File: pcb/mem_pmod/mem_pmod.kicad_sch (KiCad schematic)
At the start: 0 parts

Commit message: Start building schematic
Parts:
- added J1: Conn_01x04_Pin, symbol Connector:Conn_01x04_Pin
- added PMOD1: PMOD-Device-x2-Type-1A-GPIO, pmod-conn_6x2:pmod_pin_array_6x2, symbol pmod:PMOD-Device-x2-Type-1A-GPIO
- added U1: 74ACT139MTCX, TSSOP16_5X4P5_ONS, symbol demux:74ACT139MTCX
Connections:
- new net CS_A0: J1.2 (Pin_2), U1.2 (A0A)
- new net CS_A1: J1.3 (Pin_3), U1.3 (A1A)
- new net CS_V0: J1.4 (Pin_4), U1.14 (A0B)
- new net GND: PMOD1.11 (GND), PMOD1.5 (GND), U1.13 (A1B), U1.8 (GND)
- new net PMOD_A0: PMOD1.1 (IOA0)
- new net PMOD_A1: PMOD1.2 (IOA1)
- new net PMOD_A2: PMOD1.3 (IOA2)
- new net PMOD_A3: PMOD1.4 (IOA3)
- new net PMOD_B0: PMOD1.7 (IOB0)
- new net PMOD_B1: PMOD1.8 (IOB1)
- new net PMOD_B2: PMOD1.9 (IOB2)
- new net PMOD_B3: PMOD1.10 (IOB3)
- new net PRJ_Clock: J1.1 (Pin_1)
- new net RAM_CS0: U1.4 (*O0A)
- new net RAM_CS1: U1.5 (*O1A)
- new net RAM_CS2: U1.6 (*O2A)
- new net RAM_CS3: U1.7 (*O3A)
- new net VCC: PMOD1.12 (VCC), PMOD1.6 (VCC), U1.1 (*EA), U1.15 (*EB), U1.16 (VCC)
- new net VRAM_CS0: U1.12 (*O0B)
- new net VRAM_CS1: U1.11 (*O1B)
- no-connect marks 0 -> 2

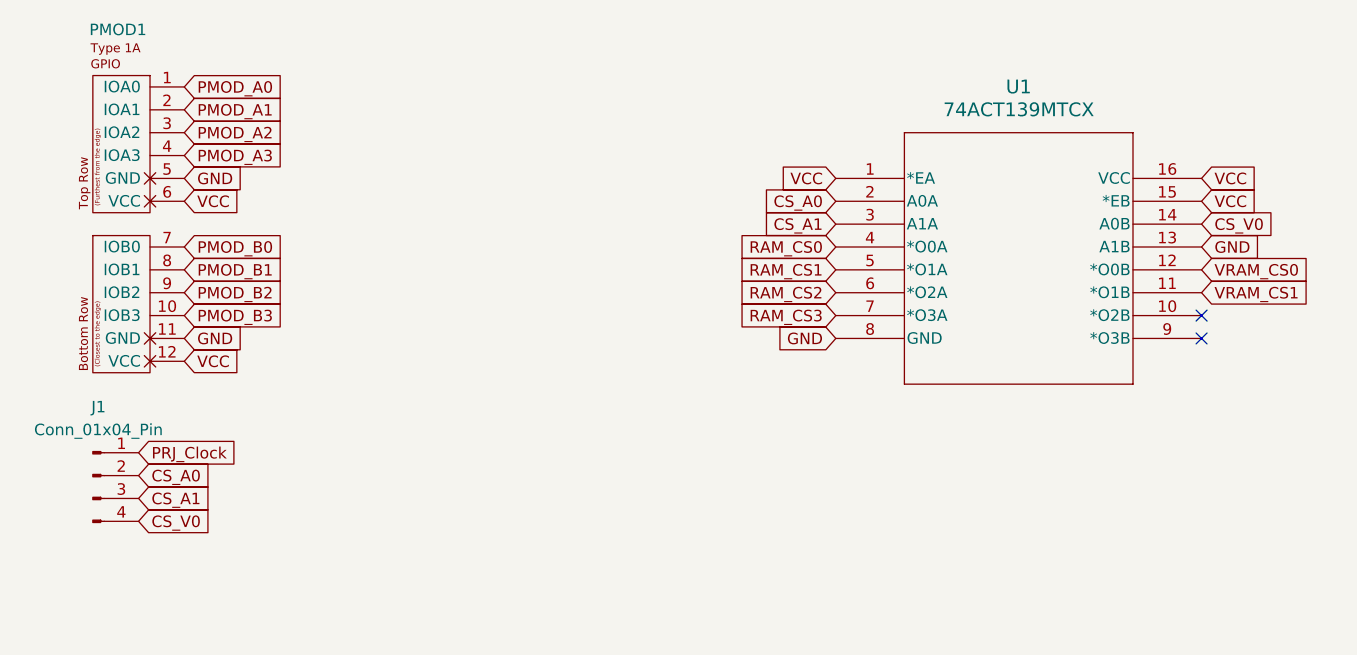
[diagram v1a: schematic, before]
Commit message: continue editing schematic
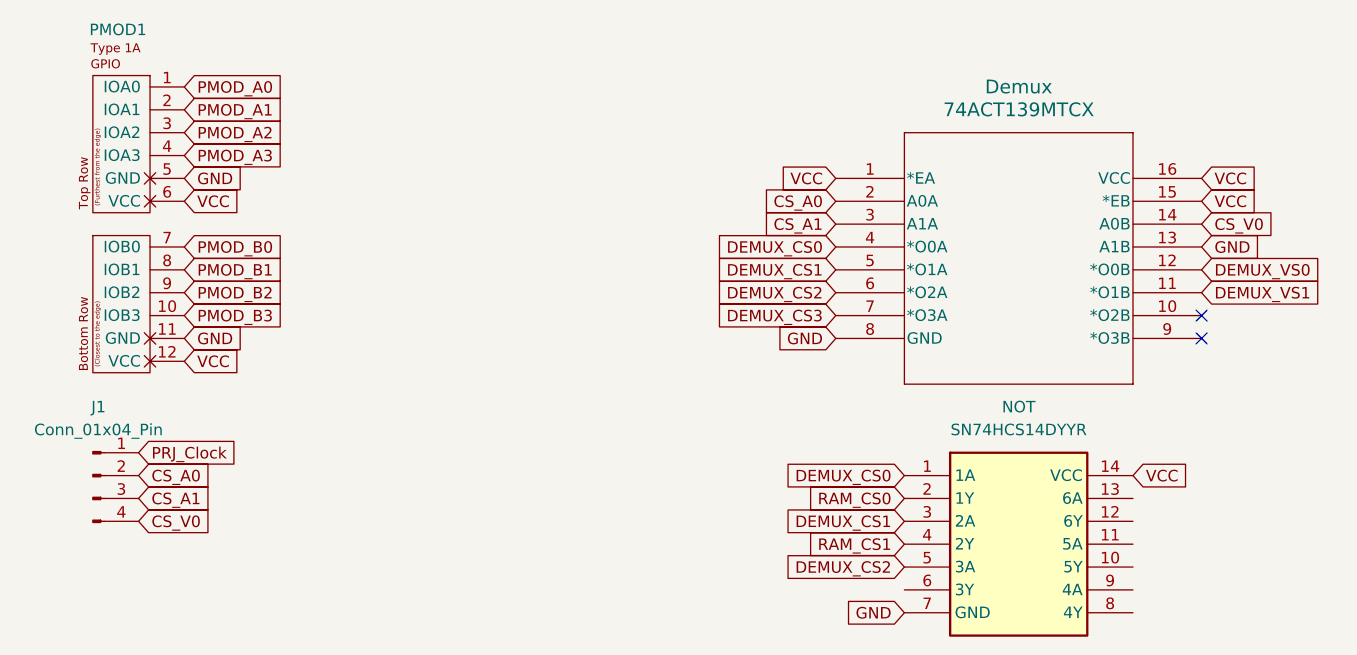
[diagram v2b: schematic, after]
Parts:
- added NOT: SN74HCS14DYYR, SOP50P326X110-14N, symbol SN74HCS14DYYR:SN74HCS14DYYR
- renumbered U1 to Demux
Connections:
- net GND: now also NOT.7 (GND)
- net RAM_CS0: now also NOT.2 (1Y); no longer Demux.4 (*O0A)
- net RAM_CS1: now also NOT.4 (2Y); no longer Demux.5 (*O1A)
- net VCC: now also NOT.14 (VCC)
- net RAM_CS2 renamed DEMUX_CS2
- net DEMUX_CS2: now also NOT.5 (3A)
- net RAM_CS3 renamed DEMUX_CS3
- net VRAM_CS0 renamed DEMUX_VS0
- net VRAM_CS1 renamed DEMUX_VS1
- new net DEMUX_CS0: Demux.4 (*O0A), NOT.1 (1A)
- new net DEMUX_CS1: Demux.5 (*O1A), NOT.3 (2A)
